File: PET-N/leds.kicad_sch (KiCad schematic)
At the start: 76 parts, among them SW1 KP "=", SW10 KP "0", SW11 R SHIFT, SW12 ">", SW14 "]", SW15 "@", SW16 L SHIFT, SW17 KP "+", SW18 KP "2", SW2 KP ".", SW20 "?", SW21 ",", SW22 "N", SW23 "V", SW24 "X", SW25 KP "3", SW26 KP "1", SW27 RETURN, SW28 ";", SW29 "M", SW3 NC ($10), SW30 "B", SW31 "C", SW32 "Z", SW320 S LOCK, SW33 KP "*", SW34 KP "5", SW36 ":", SW37 "K", SW38 "H", SW39 "F", SW4 STOP, SW40 "S", SW41 KP "6", SW42 KP "4", SW44 "L", SW45 "J", SW46 "G", SW47 "D", SW48 "A", SW49 KP "/", SW5 "<", SW50 KP "8", SW52 "P", SW53 "I", SW54 "Y", SW55 "R", SW56 "W", SW57 KP "9", SW58 KP "7", SW59 U ARROW, SW6 SPACE, SW60 "O", SW61 "U", SW62 "T", SW63 "E", SW64 "Q", SW65 INS/DEL, SW66 UP/DOWN, SW67 NC ($0A), SW68 ")", SW69 "\", SW7 "[", SW70 "'", SW71 "$", SW72 QUOTE, SW73 LEFT/RIGHT, SW74 CLR/HOME, SW75 B ARROW, SW76 "(", SW77 "&", SW78 "%", SW79 "#", SW8 OFF/RVS, SW80 "!", SW9 KP "-"

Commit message: almost done routing; last checks still open
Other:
- note added: "(C) 2020,2021 Steve J. Gray (C) 2025 André Fachat"
- note added: "CBM-KEYB-PETN-3.0-20251005"
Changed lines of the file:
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@@
 	(generator_version "9.0")
 	(paper "A4")
+	(text "CBM-KEYB-PETN-3.0-20251005"
+		(exclude_from_sim no)
+		(at 230.886 172.72 0)
+		(effects
+			(font
+				(size 4 4)
+				(thickness 0.9)
+				(bold yes)
+			)
+		)
+	)
+	(text "(C) 2020,2021 Steve J. Gray\n(C) 2025 André Fachat"
+		(exclude_from_sim no)
+		(at 249.682 181.61 0)
+		(effects
+			(font
+				(size 2.54 2.54)
+				(thickness 0.508)
+				(bold yes)
+			)
+		)
+	)
 	(junction
 		(at 125.73 115.57)

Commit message: hopefully final schem and layout for 3.0A
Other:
- note added: "CBM-KEYB-PETN-3.0A-20251011"
- note removed: "CBM-KEYB-PETN-3.0-20251005"
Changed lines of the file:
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@@
 	(generator_version "9.0")
 	(paper "A4")
-	(text "CBM-KEYB-PETN-3.0-20251005"
+	(text "CBM-KEYB-PETN-3.0A-20251011"
 		(exclude_from_sim no)
 		(at 230.886 172.72 0)

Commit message: as sent to production
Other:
- note added: "CBM-KEYB-PETN-3.0A-20251014"
- note removed: "CBM-KEYB-PETN-3.0A-20251011"
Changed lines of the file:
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@@
 	(generator_version "9.0")
 	(paper "A4")
-	(text "CBM-KEYB-PETN-3.0A-20251011"
+	(text "CBM-KEYB-PETN-3.0A-20251014"
 		(exclude_from_sim no)
 		(at 230.886 172.72 0)

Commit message: first run on r3.1
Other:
- note added: "(C) 2020, 2021 Steve J. Gray (C) 2025, 2026 André Fachat"
- note added: "CBM-KEYB-PETN-3.1A-20260130"
- note removed: "(C) 2020,2021 Steve J. Gray (C) 2025 André Fachat"
- note removed: "CBM-KEYB-PETN-3.0A-20251014"
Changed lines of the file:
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@@
 	(generator_version "9.0")
 	(paper "A4")
-	(text "CBM-KEYB-PETN-3.0A-20251014"
+	(text "CBM-KEYB-PETN-3.1A-20260130"
 		(exclude_from_sim no)
-		(at 230.886 172.72 0)
+		(at 229.87 175.26 0)
 		(effects
 			(font
-				(size 4 4)
+				(size 3.048 3.048)
 				(thickness 0.9)
 				(bold yes)
@@
 		)
 	)
-	(text "(C) 2020,2021 Steve J. Gray\n(C) 2025 André Fachat"
+	(text "(C) 2020, 2021 Steve J. Gray\n(C) 2025, 2026 André Fachat"
 		(exclude_from_sim no)
-		(at 249.682 181.61 0)
+		(at 248.666 184.15 0)
 		(effects
 			(font

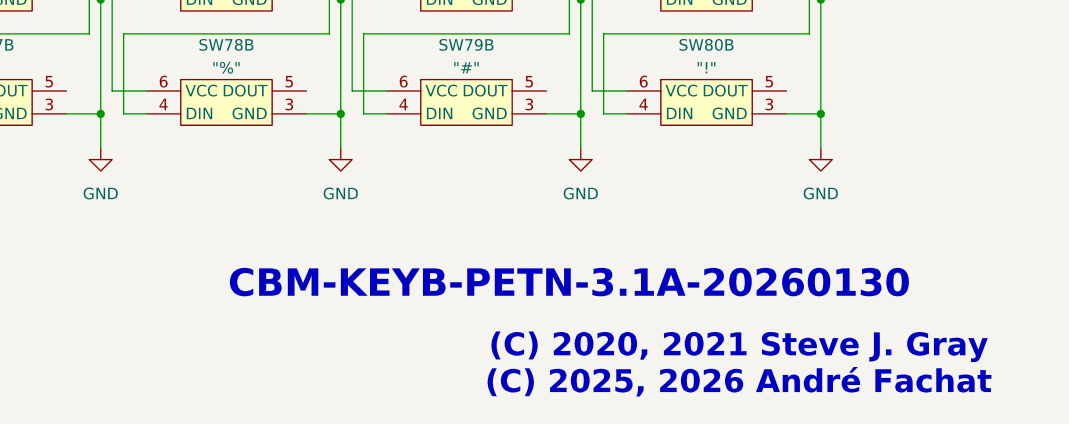
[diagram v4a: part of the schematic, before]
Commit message: add orientation marker for backlight LEDs and move to 3.1B
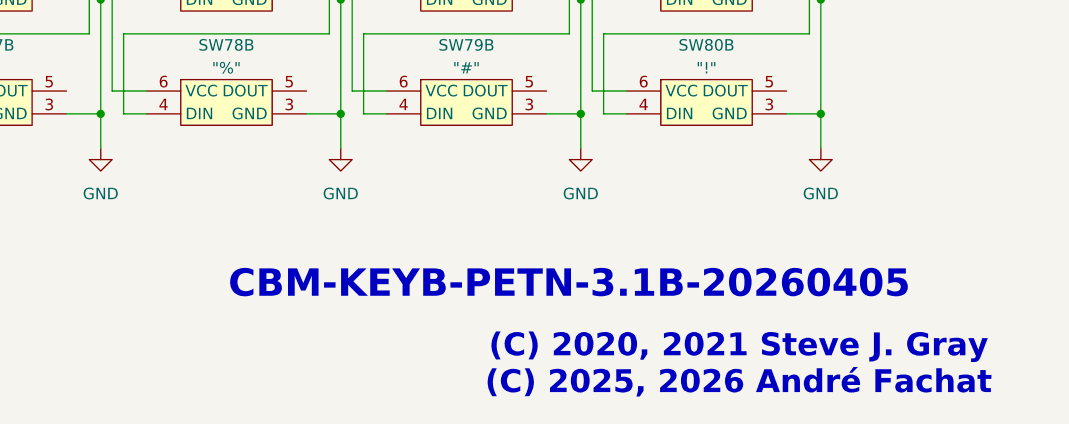
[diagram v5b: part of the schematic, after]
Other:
- note added: "CBM-KEYB-PETN-3.1B-20260405"
- note removed: "CBM-KEYB-PETN-3.1A-20260130"
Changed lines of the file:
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@@
 	(generator_version "9.0")
 	(paper "A4")
-	(text "CBM-KEYB-PETN-3.1A-20260130"
+	(text "CBM-KEYB-PETN-3.1B-20260405"
 		(exclude_from_sim no)
 		(at 229.87 175.26 0)
